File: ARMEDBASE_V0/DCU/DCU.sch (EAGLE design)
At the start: 35 parts, among them IC2 MEGA8-P, Q1 16Mhz, Q2 2N3904, Q3 2N3904

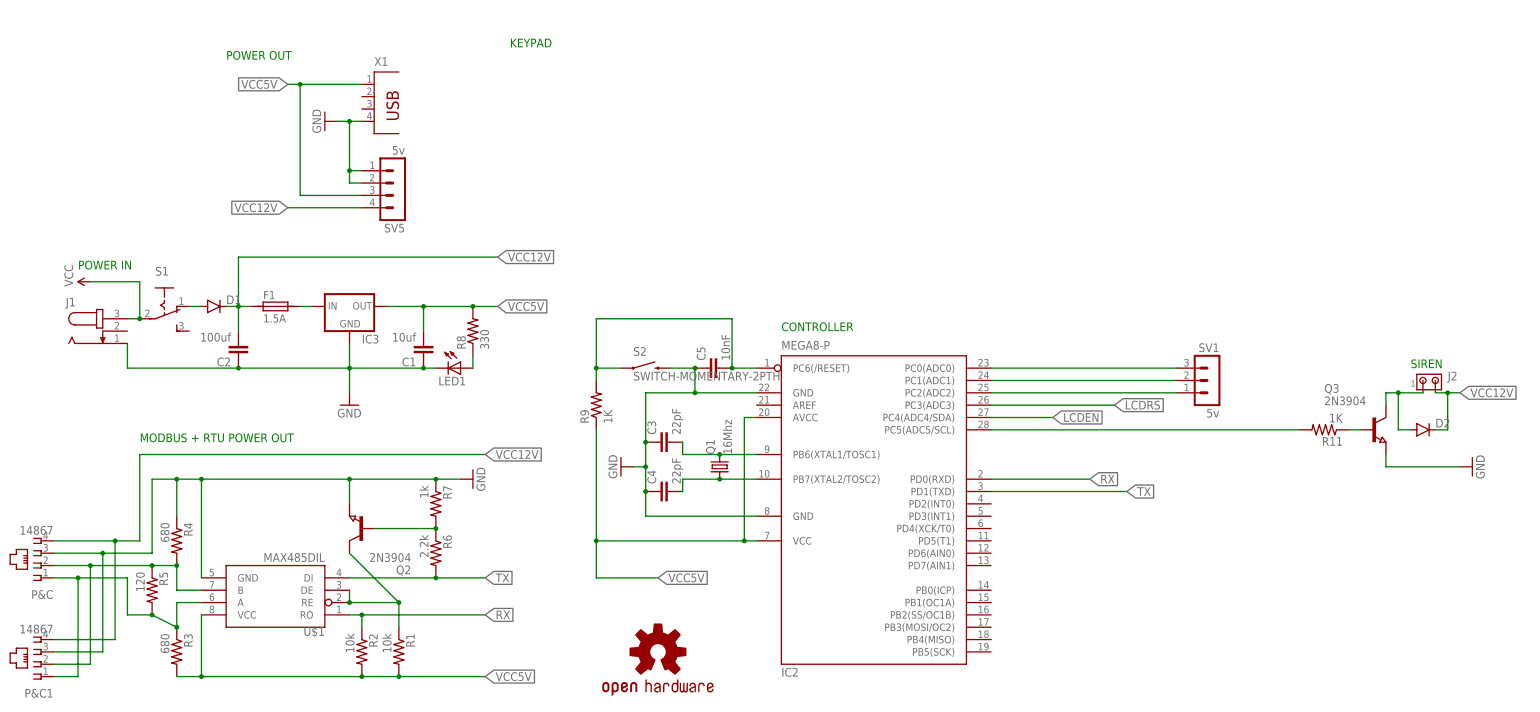
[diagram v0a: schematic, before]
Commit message: DCU
DCU seperation and CNC settings update for another shot.
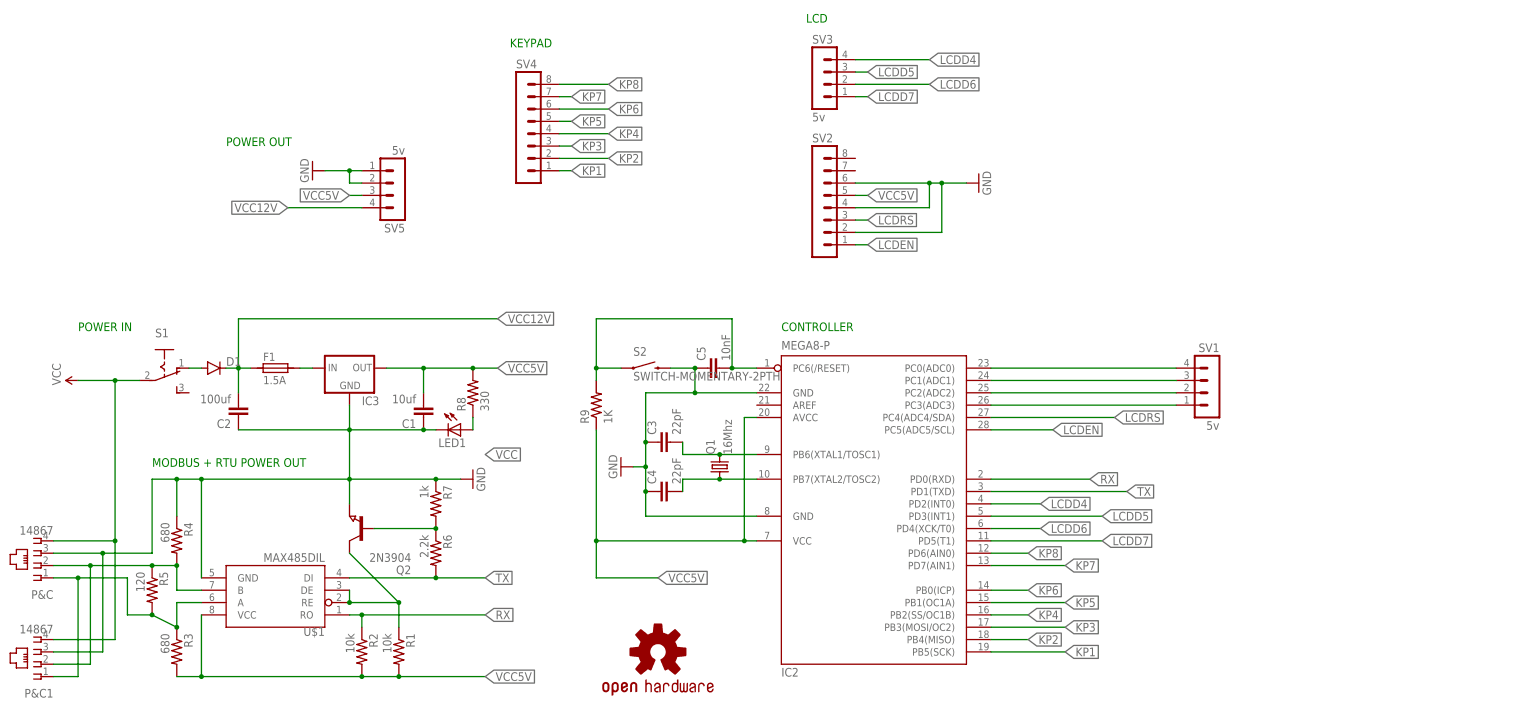
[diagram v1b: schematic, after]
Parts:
- removed D2: (no value), SparkFun-DiscreteSemi:DIODESMA
- removed J1: (no value), con-jack:JACK-PLUG1
- removed J2: (no value), con-amp:MTA02-156
- removed Q3: 2N3904, semicon-smd-ipc:NPN-TRANSISTOR_SOT23
- removed R11: 1K, SparkFun-Passives:RESISTOR0805-RES
- removed X1: (no value), con-berg:PN87520
- added SV2, SV4: (no value), con-lstb:MA08-1
- added SV3: 5v, con-lstb:MA04-1
- SV1: device con-lstb:MA03-1 -> con-lstb:MA04-1
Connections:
- removed net N$6: Q3.B, R11.1
- removed net N$9: IC2.PC5(ADC5/SCL), R11.2
- new net KP1: IC2.PB5(SCK), SV4.1
- new net KP2: IC2.PB4(MISO), SV4.2
- new net KP3: IC2.PB3(MOSI/OC2), SV4.3
- new net KP4: IC2.PB2(SS/OC1B), SV4.4
- new net KP5: IC2.PB1(OC1A), SV4.5
- new net KP6: IC2.PB0(ICP), SV4.6
- new net KP7: IC2.PD7(AIN1), SV4.7
- new net KP8: IC2.PD6(AIN0), SV4.8
- new net LCDD4: IC2.PD2(INT0), SV3.4
- new net LCDD5: IC2.PD3(INT1), SV3.3
- new net LCDD6: IC2.PD4(XCK/T0), SV3.2
- new net LCDD7: IC2.PD5(T1), SV3.1
- net GND: now also SV2.2, SV2.4, SV2.6; no longer J1.1, Q3.E, X1.4
- net LCDEN: now also IC2.PC5(ADC5/SCL), SV2.1; no longer IC2.PC4(ADC4/SDA)
- net LCDRS: now also IC2.PC4(ADC4/SDA), SV2.3; no longer IC2.PC3(ADC3)
- net N$15: now also SV1.2; no longer SV1.1
- net N$16: now also SV1.3; no longer SV1.2
- net N$17: now also SV1.4; no longer SV1.3
- net N$5: now also IC2.PC3(ADC3), SV1.1; no longer D2.A, J2.1, Q3.C
- net VCC: now also P&C.4, P&C1.4; no longer J1.3
- net VCC12V: no longer D2.C, J2.2, P&C.4, P&C1.4
- net VCC5V: now also SV2.5; no longer X1.1
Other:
- note added: "LCD"
- note removed: "SIREN"
- moved on the sheet: C1, C2, D1, F1, IC3, LED1, R8, S1
